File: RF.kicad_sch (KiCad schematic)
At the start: 28 parts, among them J1 Conn_Coaxial, SW1 SW_DIP_x01, U1 AD8307, U2 L7805

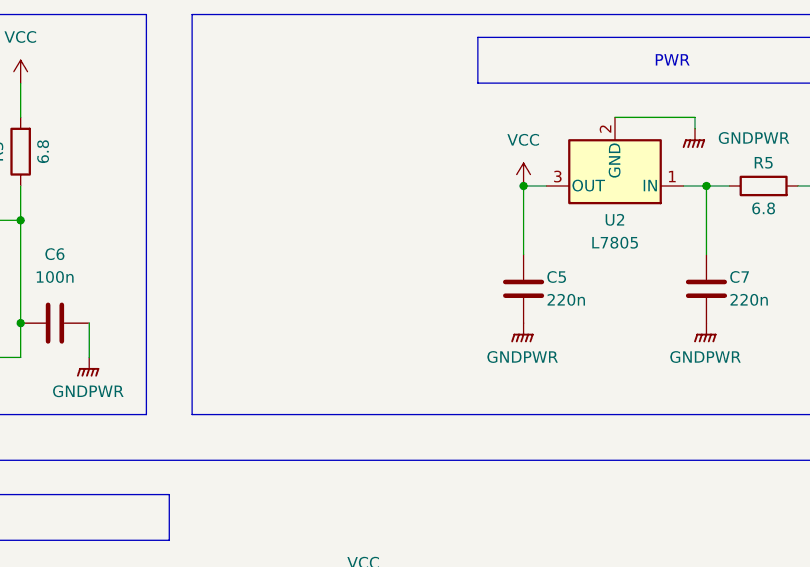
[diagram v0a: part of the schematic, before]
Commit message: dodany kondensator na wyjściu VRM
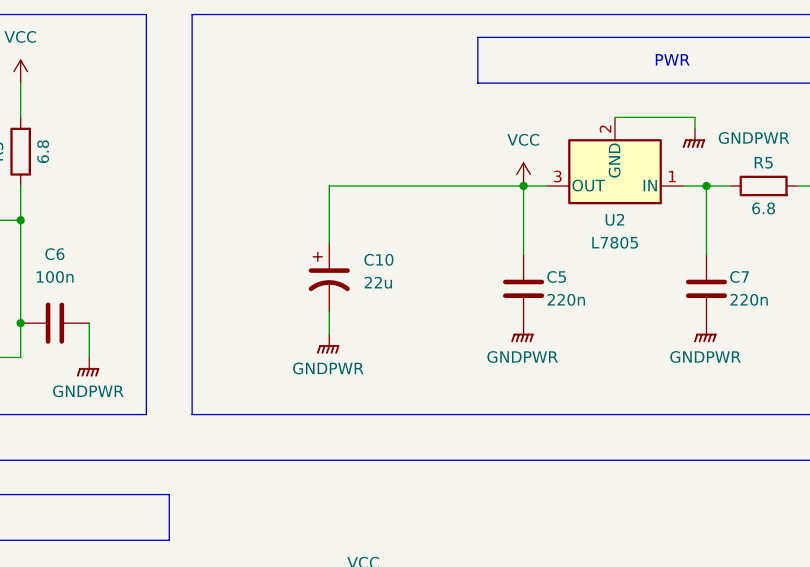
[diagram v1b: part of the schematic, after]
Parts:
- added C10: 22u, Capacitor_SMD:CP_Elec_10x7.7, symbol Device:C_Polarized_US
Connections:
- net GNDPWR: now also C10.2
- net VCC: now also C10.1
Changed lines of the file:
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@@
+	(wire
+		(pts
+			(xy 212.09 34.29) (xy 190.5 34.29)
+		)
+		(stroke
+			(width 0)
+			(type default)
+		)
+	)
 	(wire
 		(pts
@@
 	(wire
 		(pts
+			(xy 190.5 48.26) (xy 190.5 50.8)
+		)
+		(stroke
+			(width 0)
+			(type default)
+		)
+	)
+	(wire
+		(pts
 			(xy 232.41 34.29) (xy 232.41 41.91)
 		)
@@
 		(pts
 			(xy 204.47 102.87) (xy 208.28 102.87)
+		)
+		(stroke
+			(width 0)
+			(type default)
+		)
+	)
+	(wire
+		(pts
+			(xy 190.5 34.29) (xy 190.5 40.64)
 		)
 		(stroke
@@
 	)
 	(symbol
+		(lib_id "Device:C_Polarized_US")
+		(at 190.5 44.45 0)
+		(unit 1)
+		(exclude_from_sim no)
+		(in_bom yes)
+		(on_board yes)
+		(dnp no)
+		(fields_autoplaced yes)
+		(property "Reference" "C10"
+			(at 194.31 42.5449 0)
+			(effects
+				(font
+					(size 1.27 1.27)
+				)
+				(justify left)
+			)
+		)
+		(property "Value" "22u"
+			(at 194.31 45.0849 0)
+			(effects
+				(font
+					(size 1.27 1.27)
+				)
+				(justify left)
+			)
+		)
+		(property "Footprint" "Capacitor_SMD:CP_Elec_10x7.7"
+			(at 190.5 44.45 0)
+			(effects
+				(font
+					(size 1.27 1.27)
+				)
+				(hide yes)
+			)
+		)
+		(property "Datasheet" "~"
+			(at 190.5 44.45 0)
+			(effects
+				(font
+					(size 1.27 1.27)
+				)
+				(hide yes)
+			)
+		)
+		(property "Description" "Polarized capacitor, US symbol"
+			(at 190.5 44.45 0)
+			(effects
+				(font
+					(size 1.27 1.27)
+				)
+				(hide yes)
+			)
+		)
+		(pin "1"
+		)
+		(pin "2"
+		)
+		(instances
+			(project ""
+				(path "/6e9b0ecb-5ff8-4cea-bb01-e8c92e636c95/09627191-d48d-42a8-a392-355888bdeeaa"
+					(reference "C10")
+					(unit 1)
+				)
+			)
+		)
+	)
+	(symbol
 		(lib_id "power:GNDPWR")
 		(at 69.85 111.76 0)
@@
 					(unit 1)
 				)
+			)
+		)
+	)
+	(symbol
+		(lib_id "power:GNDPWR")
+		(at 190.5 50.8 0)
+		(unit 1)
+		(exclude_from_sim no)
+		(in_bom yes)
+		(on_board yes)
+		(dnp no)
+		(fields_autoplaced yes)
+		(property "Reference" "#PWR025"
+			(at 190.5 55.88 0)
+			(effects
+				(font
+					(size 1.27 1.27)
+				)
+				(hide yes)
+			)
+		)
+		(property "Value" "GNDPWR"
+			(at 190.373 54.61 0)
+			(effects
+				(font
+					(size 1.27 1.27)
+				)
+			)
+		)
+		(property "Footprint" ""
+			(at 190.5 52.07 0)
+			(effects
+				(font
+					(size 1.27 1.27)
+				)
+				(hide yes)
+			)
+		)
+		(property "Datasheet" ""
+			(at 190.5 52.07 0)
+			(effects
+				(font
+					(size 1.27 1.27)
+				)
+				(hide yes)
+			)
+		)
+		(property "Description" "Power symbol creates a global label with name \"GNDPWR\" , global ground"
+			(at 190.5 50.8 0)
+			(effects
+				(font
+					(size 1.27 1.27)
+				)
+				(hide yes)
+			)
+		)
+		(pin "1"
+		)
+		(instances
+			(project ""
+				(path "/6e9b0ecb-5ff8-4cea-bb01-e8c92e636c95/09627191-d48d-42a8-a392-355888bdeeaa"
+					(reference "#PWR025")
+					(unit 1)
+				)
